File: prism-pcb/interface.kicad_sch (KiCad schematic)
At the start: 17 parts, among them J301 Conn_01x04_P3.5mm_TBH_Horizon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, M301 Fan_5VDC_25x25x8mm, U301 TPSM365R6V5RDNR, U302 LTC6820HMS-TRPBF

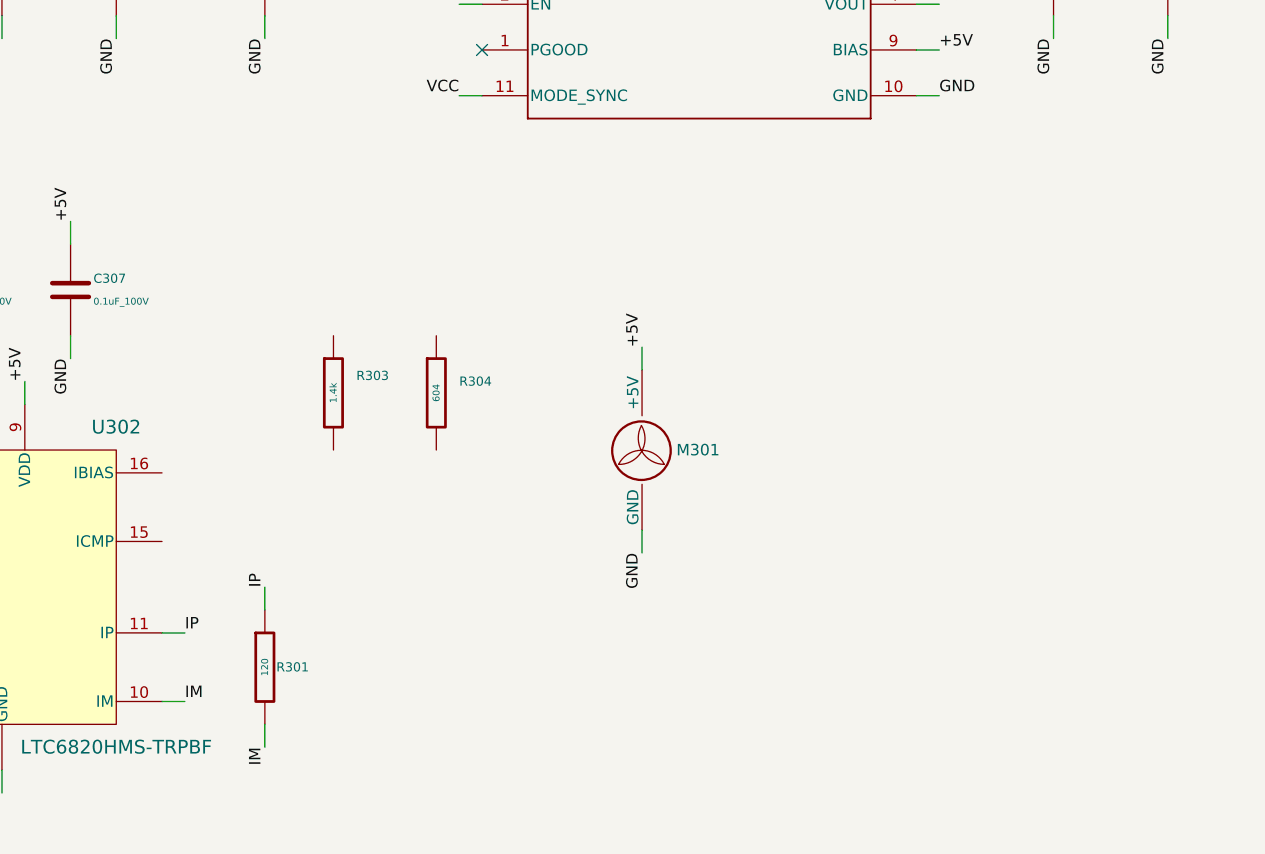
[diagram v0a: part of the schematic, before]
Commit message: Add transformer and choke
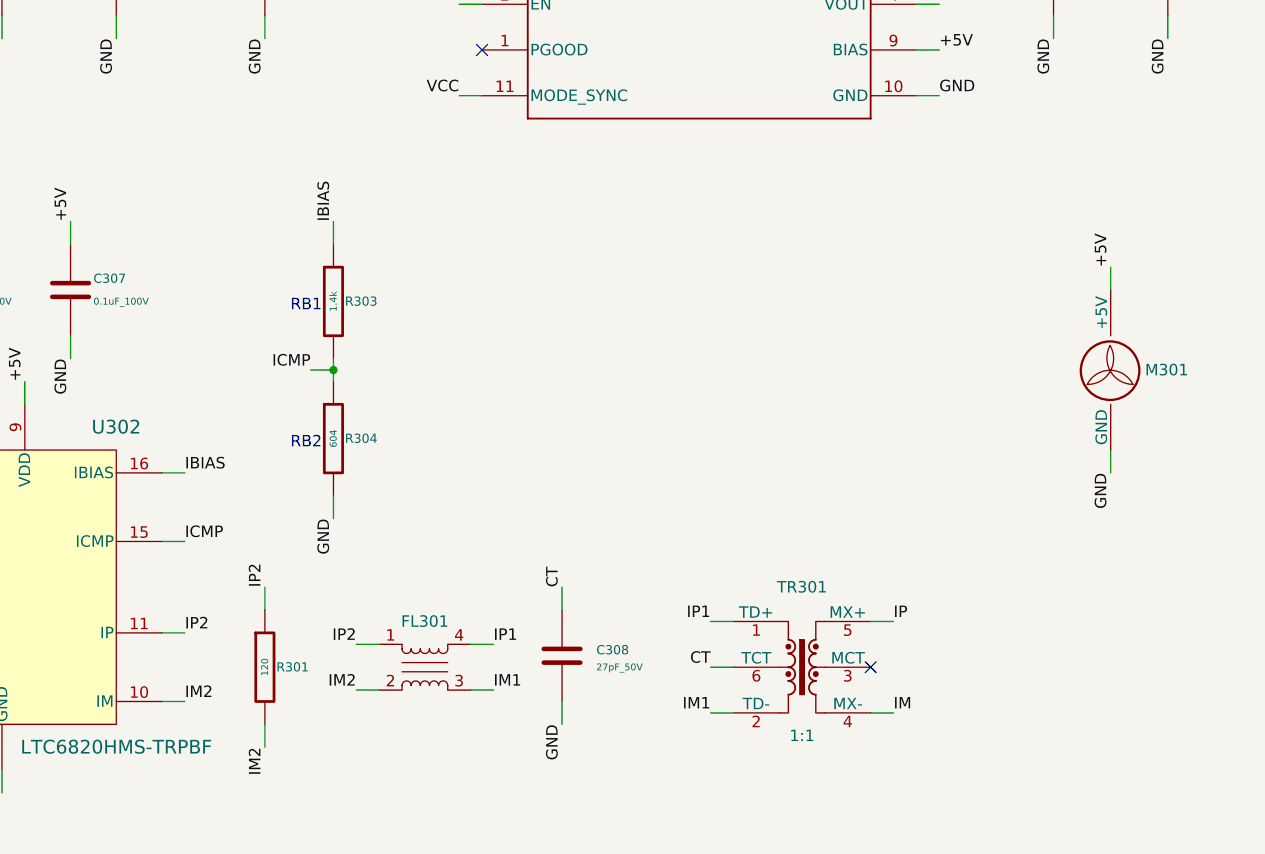
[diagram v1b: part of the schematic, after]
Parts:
- added C308: 27pF_50V, Janelia:C_0402_1005Metric, symbol Janelia:C_27pF_50V_0402
- added FL301: Choke_CMF_ACT45B-220-2P, Janelia:SMD_0-2P-TL003_TDK-L, symbol Janelia:Choke_CMF_ACT45B-220-2P
- added TR301: 1:1, Janelia:FB020G00, symbol Janelia:Transformer_Pulse_1CT{colon}1CT_SMD
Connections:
- net GND: now also R304.2, C308.2
- net IM: now also TR301.4 (MX-); no longer R301.2, U302.10 (IM)
- net IP: now also TR301.5 (MX+); no longer R301.1, U302.11 (IP)
- net ICMP: now reaches U302.15 (ICMP)
- net ICMP: now also R303.2, R304.1
- net IBIAS: now reaches U302.16 (IBIAS)
- net IBIAS: now also R303.1
- new net CT: C308.1, TR301.6 (TCT)
- new net IM1: FL301.3, TR301.2 (TD-)
- new net IM2: FL301.2, R301.2, U302.10 (IM)
- new net IP1: FL301.4, TR301.1 (TD+)
- new net IP2: FL301.1, R301.1, U302.11 (IP)
- no-connect marks 4 -> 5
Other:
- note added: "RB1"
- note added: "RB2"
- moved on the sheet: M301, R303, R304

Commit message: Finish v2.0 layout
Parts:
- added R305: 100k, Janelia:R_0402_1005Metric, symbol Janelia:R_100k_0402
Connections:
- net +5V: now also R305.1
- net COPI: now also R305.2
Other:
- note added: "LTC6280 COPI IS OPEN DRAIN THIS RESISTOR PERHAPS UNNECESSARY TMC5130 COPI HAS PULL-UP"
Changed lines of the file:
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@@
   (title_block
     (title "prism-pcb")
-    (date "2024-09-18")
+    (date "2024-09-20")
     (rev "2.0")
     (company "Howard Hughes Medical Institute")
@@
     (stroke (width 0) (type default))
   )
+  (wire (pts (xy 63.5 142.24) (xy 63.5 139.7))
+    (stroke (width 0) (type default))
+  )
   (wire (pts (xy 196.85 139.7) (xy 194.31 139.7))
     (stroke (width 0) (type default))
@@
     (stroke (width 0) (type default))
   )
+  (wire (pts (xy 57.15 66.04) (xy 59.69 66.04))
+    (stroke (width 0) (type default))
+  )
   (wire (pts (xy 152.4 111.76) (xy 152.4 113.03))
     (stroke (width 0) (type default))
@@
     (stroke (width 0) (type default))
   )
+  (wire (pts (xy 63.5 127) (xy 63.5 124.46))
+    (stroke (width 0) (type default))
+  )
   (wire (pts (xy 133.35 123.19) (xy 135.89 123.19))
     (stroke (width 0) (type default))
@@
     (effects (font (size 1.27 1.27)) (justify right bottom))
   )
+  (text "LTC6280 COPI IS OPEN DRAIN\nTHIS RESISTOR PERHAPS UNNECESSARY\nTMC5130 COPI HAS PULL-UP"
+    (at 62.23 137.16 0)
+    (effects (font (size 1.27 1.27)) (justify right bottom))
+  )
   (text "FAST MODE" (at 90.17 125.73 0)
     (effects (font (size 1.27 1.27)) (justify right bottom))
@@
     (effects (font (size 1.27 1.27)) (justify right bottom))
   )
+  (label "COPI" (at 63.5 142.24 270) (fields_autoplaced)
+    (effects (font (size 1.27 1.27)) (justify right bottom))
+  )
   (label "GND" (at 115.57 43.18 270) (fields_autoplaced)
     (effects (font (size 1.27 1.27)) (justify right bottom))
@@
     (effects (font (size 1.27 1.27)) (justify right bottom))
   )
+  (label "COPI" (at 57.15 66.04 180) (fields_autoplaced)
+    (effects (font (size 1.27 1.27)) (justify right bottom))
+  )
   (label "ICMP" (at 135.89 130.81 0) (fields_autoplaced)
     (effects (font (size 1.27 1.27)) (justify left bottom))
@@
     (effects (font (size 1.27 1.27)) (justify right bottom))
   )
+  (label "+5V" (at 63.5 124.46 90) (fields_autoplaced)
+    (effects (font (size 1.27 1.27)) (justify left bottom))
+  )
   (label "VCC" (at 144.78 59.69 90) (fields_autoplaced)
     (effects (font (size 1.27 1.27)) (justify left bottom))
+  )
+  (label "COPI" (at 95.25 140.97 180) (fields_autoplaced)
+    (effects (font (size 1.27 1.27)) (justify right bottom))
   )
   (label "VCC" (at 166.37 81.28 180) (fields_autoplaced)
@@
     (effects (font (size 1.27 1.27)) (justify right))
   )
-  (hierarchical_label "COPI" (shape output) (at 95.25 140.97 180) (fields_autoplaced)
-    (effects (font (size 1.27 1.27)) (justify right))
+  (hierarchical_label "COPI" (shape output) (at 59.69 66.04 0) (fields_autoplaced)
+    (effects (font (size 1.27 1.27)) (justify left))
   )
   (hierarchical_label "VAA" (shape passive) (at 59.69 58.42 0) (fields_autoplaced)
@@
         )
       )
+    )
+  )
+  (symbol (lib_id "Janelia:R_100k_0402") (at 63.5 133.35 0) (unit 1)
+    (in_bom yes) (on_board yes) (dnp no)
+    (property "Reference" "R305" (at 64.77 133.35 0) (do_not_autoplace)
+      (effects (font (size 1.016 1.016)) (justify left))
+    )
+    (property "Value" "100k" (at 63.5 133.35 90) (do_not_autoplace)
+      (effects (font (size 0.762 0.762)))
+    )
+    (property "Footprint" "Janelia:R_0402_1005Metric" (at 61.722 133.35 90)
+      (effects (font (size 0.762 0.762)) hide)
+    )
+    (property "Datasheet" "" (at 65.532 133.35 90)
+      (effects (font (size 0.762 0.762)) hide)
+    )
+    (property "Vendor" "Digi-Key" (at 68.072 130.81 90)
+      (effects (font (size 1.524 1.524)) hide)
+    )
+    (property "Vendor Part Number" "311-100KJRCT-ND" (at 70.612 128.27 90)
+      (effects (font (size 1.524 1.524)) hide)
+    )
+    (property "Synopsis" "RES 100K OHM 5% 1/16W" (at 73.152 125.73 90)
+      (effects (font (size 1.524 1.524)) hide)
+    )
+    (property "Manufacturer" "YAGEO" (at 63.5 133.35 0)
+      (effects (font (size 1.27 1.27)) hide)
+    )
+    (property "Manufacturer Part Number" "RC0402JR-07100KL" (at 63.5 133.35 0)
+      (effects (font (size 1.27 1.27)) hide)
+    )
+    (property "Package" "0402" (at 63.5 133.35 0)
+      (effects (font (size 1.27 1.27)) hide)
+    )
+    (property "LCSC" "C106234" (at 63.5 133.35 0)
+      (effects (font (size 1.27 1.27)) hide)
+    )
+    (pin "1")
+    (pin "2")
+    (instances
+      (project "prism-pcb"
+        (path "/df2b2e89-e055-4140-95de-f1df723db034/c1dd8f61-494c-402f-8e59-08309c64fc3f"
+          (reference "R305") (unit 1)
+        )
+      )

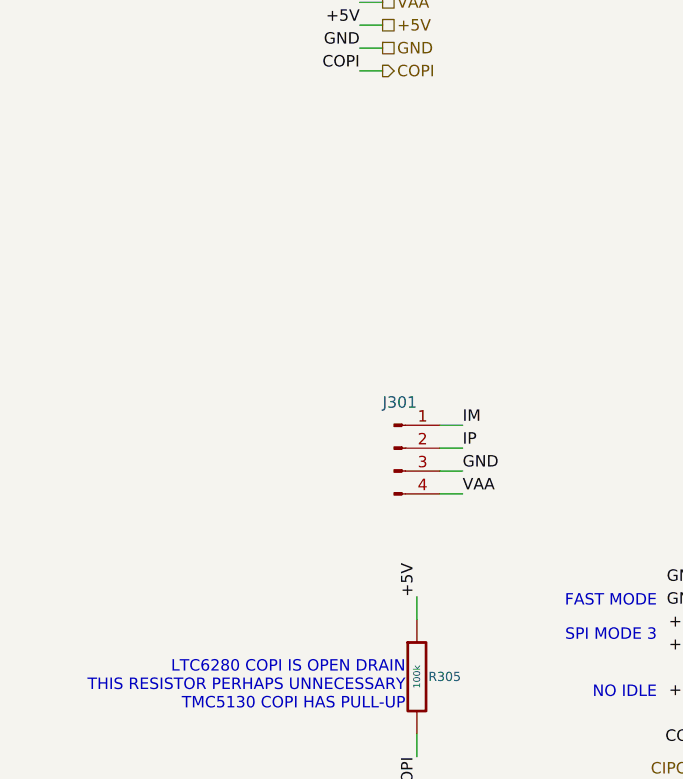
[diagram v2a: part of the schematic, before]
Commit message: Switch to USB connector
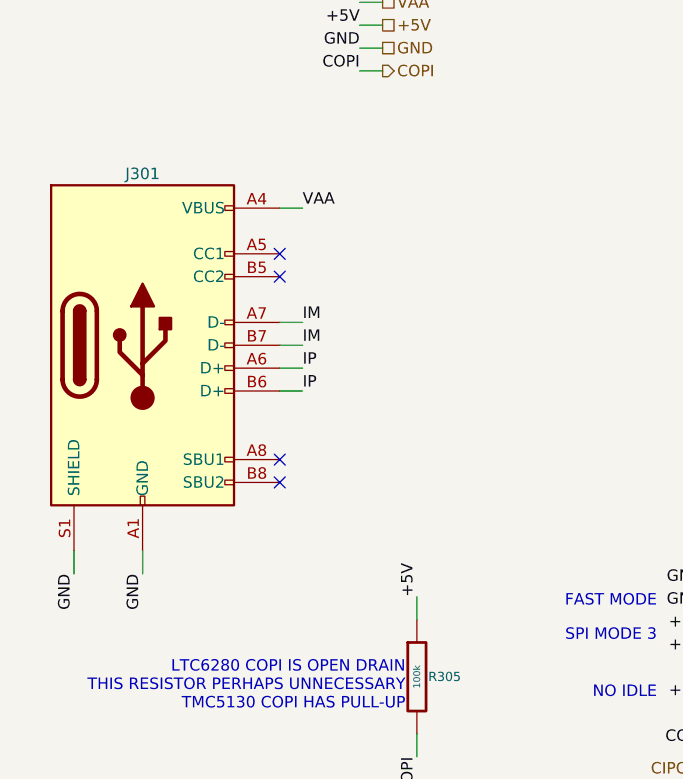
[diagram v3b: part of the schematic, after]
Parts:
- removed J301: Conn_01x04_P3.5mm_TBH_Horizontal_Screw, Janelia:PhoenixContact_MC_1,5_4-G-3.5_1x04_P3.50mm_Horizontal_Screw, symbol Janelia:Conn_01x04_P3.5mm_TBH_Horizontal_Screw
- added J301: USB_C_Receptacle_USB2.0_16P_GT-USB-7047C, Janelia:USB_C_Receptacle_GT-USB-7047C_16P_TopMnt_Horizontal, symbol Janelia:USB_C_Receptacle_USB2.0_16P_GT-USB-7047C
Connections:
- net GND: now also J301.A1 (GND), J301.A12 (GND), J301.B1 (GND), J301.B12 (GND), J301.S1 (SHIELD)
- net IM: now also J301.A7 (D-), J301.B7 (D-)
- net IP: now also J301.A6 (D+), J301.B6 (D+)
- net VAA: now also J301.A4 (VBUS), J301.A9 (VBUS), J301.B4 (VBUS), J301.B9 (VBUS)
- no-connect marks 5 -> 9
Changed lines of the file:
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@@
   (title_block
     (title "prism-pcb")
-    (date "2024-09-20")
+    (date "2024-09-23")
     (rev "2.0")
     (company "Howard Hughes Medical Institute")
@@
   (junction (at 152.4 111.76) (diameter 0) (color 0 0 0 0)
   )
+  (no_connect (at 48.26 86.36))
+  (no_connect (at 48.26 111.76))
   (no_connect (at 212.09 144.78))
   (no_connect (at 217.17 63.5))
   (no_connect (at 217.17 66.04))
   (no_connect (at 168.91 76.2))
+  (no_connect (at 48.26 88.9))
   (no_connect (at 217.17 58.42))
+  (no_connect (at 48.26 109.22))
   (wire (pts (xy 97.79 135.89) (xy 95.25 135.89))
     (stroke (width 0) (type default))
@@
     (stroke (width 0) (type default))
   )
-  (wire (pts (xy 66.04 110.49) (xy 68.58 110.49))
+  (wire (pts (xy 33.02 119.38) (xy 33.02 121.92))
     (stroke (width 0) (type default))
   )
@@
     (stroke (width 0) (type default))
   )
-  (wire (pts (xy 66.04 105.41) (xy 68.58 105.41))
+  (wire (pts (xy 48.26 93.98) (xy 50.8 93.98))
     (stroke (width 0) (type default))
   )
@@
     (stroke (width 0) (type default))
   )
+  (wire (pts (xy 25.4 119.38) (xy 25.4 121.92))
+    (stroke (width 0) (type default))
+  )
   (wire (pts (xy 157.48 147.32) (xy 154.94 147.32))
     (stroke (width 0) (type default))
@@
     (stroke (width 0) (type default))
   )
-  (wire (pts (xy 66.04 113.03) (xy 68.58 113.03))
+  (wire (pts (xy 48.26 81.28) (xy 50.8 81.28))
     (stroke (width 0) (type default))
   )
@@
     (stroke (width 0) (type default))
   )
-  (wire (pts (xy 66.04 107.95) (xy 68.58 107.95))
+  (wire (pts (xy 48.26 101.6) (xy 50.8 101.6))
+    (stroke (width 0) (type default))
+  )
+  (wire (pts (xy 48.26 96.52) (xy 50.8 96.52))
     (stroke (width 0) (type default))
   )
   (wire (pts (xy 115.57 62.23) (xy 115.57 59.69))
+    (stroke (width 0) (type default))
+  )
+  (wire (pts (xy 48.26 99.06) (xy 50.8 99.06))
     (stroke (width 0) (type default))
   )
@@
     (effects (font (size 1.27 1.27)) (justify right bottom))
   )
-  (label "IP" (at 68.58 107.95 0) (fields_autoplaced)
-    (effects (font (size 1.27 1.27)) (justify left bottom))
+  (label "IP" (at 50.8 101.6 0) (fields_autoplaced)
+    (effects (font (size 1.27 1.27)) (justify left bottom))
+  )
+  (label "GND" (at 25.4 121.92 270) (fields_autoplaced)
+    (effects (font (size 1.27 1.27)) (justify right bottom))
   )
   (label "IM2" (at 154.94 147.32 180) (fields_autoplaced)
@@
     (effects (font (size 1.27 1.27)) (justify left bottom))
   )
-  (label "IM" (at 68.58 105.41 0) (fields_autoplaced)
+  (label "IM" (at 50.8 93.98 0) (fields_autoplaced)
     (effects (font (size 1.27 1.27)) (justify left bottom))
   )
@@
     (effects (font (size 1.27 1.27)) (justify right bottom))
   )
+  (label "IP" (at 50.8 99.06 0) (fields_autoplaced)
+    (effects (font (size 1.27 1.27)) (justify left bottom))
+  )
   (label "GND" (at 115.57 74.93 270) (fields_autoplaced)
     (effects (font (size 1.27 1.27)) (justify right bottom))
@@
     (effects (font (size 1.27 1.27)) (justify right bottom))
   )
-  (label "VAA" (at 68.58 113.03 0) (fields_autoplaced)
-    (effects (font (size 1.27 1.27)) (justify left bottom))
-  )
-  (label "GND" (at 68.58 110.49 0) (fields_autoplaced)
-    (effects (font (size 1.27 1.27)) (justify left bottom))
+  (label "VAA" (at 50.8 81.28 0) (fields_autoplaced)
+    (effects (font (size 1.27 1.27)) (justify left bottom))
+  )
+  (label "GND" (at 33.02 121.92 270) (fields_autoplaced)
+    (effects (font (size 1.27 1.27)) (justify right bottom))
   )
   (label "IP2" (at 154.94 142.24 180) (fields_autoplaced)
@@
   (label "COPI" (at 95.25 140.97 180) (fields_autoplaced)
     (effects (font (size 1.27 1.27)) (justify right bottom))
+  )
+  (label "IM" (at 50.8 96.52 0) (fields_autoplaced)
+    (effects (font (size 1.27 1.27)) (justify left bottom))
   )
   (label "VCC" (at 166.37 81.28 180) (fields_autoplaced)
@@
     )
   )
-  (symbol (lib_id "Janelia:Conn_01x04_P3.5mm_TBH_Horizontal_Screw") (at 60.96 107.95 0) (unit 1)
-    (in_bom yes) (on_board yes) (dnp no) (fields_autoplaced)
-    (property "Reference" "J301" (at 61.595 102.87 0)
-      (effects (font (size 1.27 1.27)))
-    )
-    (property "Value" "Conn_01x04_P3.5mm_TBH_Horizontal_Screw" (at 60.96 120.65 0)
-      (effects (font (size 1.27 1.27)) hide)
-    )
-    (property "Footprint" "Janelia:PhoenixContact_MC_1,5_4-G-3.5_1x04_P3.50mm_Horizontal_Screw" (at 60.96 72.39 0)
-      (effects (font (size 1.27 1.27)) hide)
-    )
-    (property "Datasheet" "" (at 60.96 87.63 0)
-      (effects (font (size 1.27 1.27)) hide)
-    )
-    (property "Manufacturer" "Phoenix Contact" (at 60.96 74.93 0)
-      (effects (font (size 1.27 1.27)) hide)
-    )
-    (property "Manufacturer Part Number" "1844236" (at 60.96 80.01 0)
-      (effects (font (size 1.27 1.27)) hide)
-    )
-    (property "Synopsis" "TERM BLOCK HDR 4POS 90DEG 3.5MM" (at 60.96 82.55 0)
-      (effects (font (size 1.27 1.27)) hide)
-    )
-    (property "Vendor" "Digi-Key" (at 60.96 77.47 0)
-      (effects (font (size 1.27 1.27)) hide)
-    )
-    (property "Vendor Part Number" "277-2419-ND" (at 60.96 85.09 0)
-      (effects (font (size 1.27 1.27)) hide)
-    )
-    (property "Sim.Enable" "0" (at 60.96 107.95 0)
-      (effects (font (size 1.27 1.27)) hide)
-    )
-    (property "LCSC" "C480590" (at 60.96 107.95 0)
-      (effects (font (size 1.27 1.27)) hide)
-    )
-    (property "Package" "Push-Pull P=3.5mm" (at 60.96 107.95 0)
-      (effects (font (size 1.27 1.27)) hide)
-    )
-    (pin "1")
-    (pin "2")
-    (pin "4")
-    (pin "3")
-    (instances
-      (project "prism-pcb"
-        (path "/df2b2e89-e055-4140-95de-f1df723db034/c1dd8f61-494c-402f-8e59-08309c64fc3f"
-          (reference "J301") (unit 1)
-        )
-      )
-    )
-  )
   (symbol (lib_id "Janelia:R_1.4k_0402") (at 152.4 104.14 0) (unit 1)
     (in_bom yes) (on_board yes) (dnp no)
@@
         )
       )
+    )
+  )
+  (symbol (lib_id "Janelia:USB_C_Receptacle_USB2.0_16P_GT-USB-7047C") (at 33.02 96.52 0) (unit 1)
+    (in_bom yes) (on_board yes) (dnp no)
+    (property "Reference" "J301" (at 33.02 77.47 0)
+      (effects (font (size 1.27 1.27)))
+    )
+    (property "Value" "USB_C_Receptacle_USB2.0_16P_GT-USB-7047C" (at 33.02 76.835 0)
+      (effects (font (size 1.27 1.27)) hide)
+    )
+    (property "Footprint" "Janelia:USB_C_Receptacle_GT-USB-7047C_16P_TopMnt_Horizontal" (at 36.83 96.52 0)
+      (effects (font (size 1.27 1.27)) hide)
+    )
+    (property "Datasheet" "" (at 36.83 96.52 0)
+      (effects (font (size 1.27 1.27)) hide)
+    )
+    (property "Synopsis" "USB Type-C 2.0 16P 5A" (at 33.02 96.52 0)
+      (effects (font (size 1.27 1.27)) hide)
+    )
+    (property "Package" "SMD" (at 33.02 96.52 0)
+      (effects (font (size 1.27 1.27)) hide)
+    )
+    (property "Manufacturer" "G-Switch" (at 33.02 96.52 0)
+      (effects (font (size 1.27 1.27)) hide)
+    )
+    (property "Manufacturer Part Number" "GT-USB-7047C" (at 33.02 96.52 0)
+      (effects (font (size 1.27 1.27)) hide)
+    )
+    (property "Vendor" "JLCPCB" (at 33.02 96.52 0)
+      (effects (font (size 1.27 1.27)) hide)
+    )
+    (property "Vendor Part Number" "C963218" (at 33.02 96.52 0)
+      (effects (font (size 1.27 1.27)) hide)
+    )
+    (property "LCSC" "C963218" (at 33.02 96.52 0)
+      (effects (font (size 1.27 1.27)) hide)
+    )
+    (pin "B8")
+    (pin "B5")
+    (pin "B4")
+    (pin "B1")
+    (pin "B9")
+    (pin "S1")
+    (pin "B12")
+    (pin "A7")
+    (pin "A8")
+    (pin "A6")
+    (pin "A4")
+    (pin "A5")
+    (pin "A1")
+    (pin "A12")
+    (pin "A9")
+    (pin "B6")
+    (pin "B7")
+    (instances
+      (project "prism-pcb"
+        (path "/df2b2e89-e055-4140-95de-f1df723db034/c1dd8f61-494c-402f-8e59-08309c64fc3f"
+          (reference "J301") (unit 1)
+        )
+      )
